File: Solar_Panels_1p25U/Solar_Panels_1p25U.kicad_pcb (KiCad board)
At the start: 2 copper layers, 113 x 82.5 mm, 62 parts, among them J1 Conn_01x08_MountingPin, J2 Conn_01x08_MountingPin, J3 Conn_01x08_MountingPin, J4 Conn_01x02, J5 Conn_01x08_MountingPin

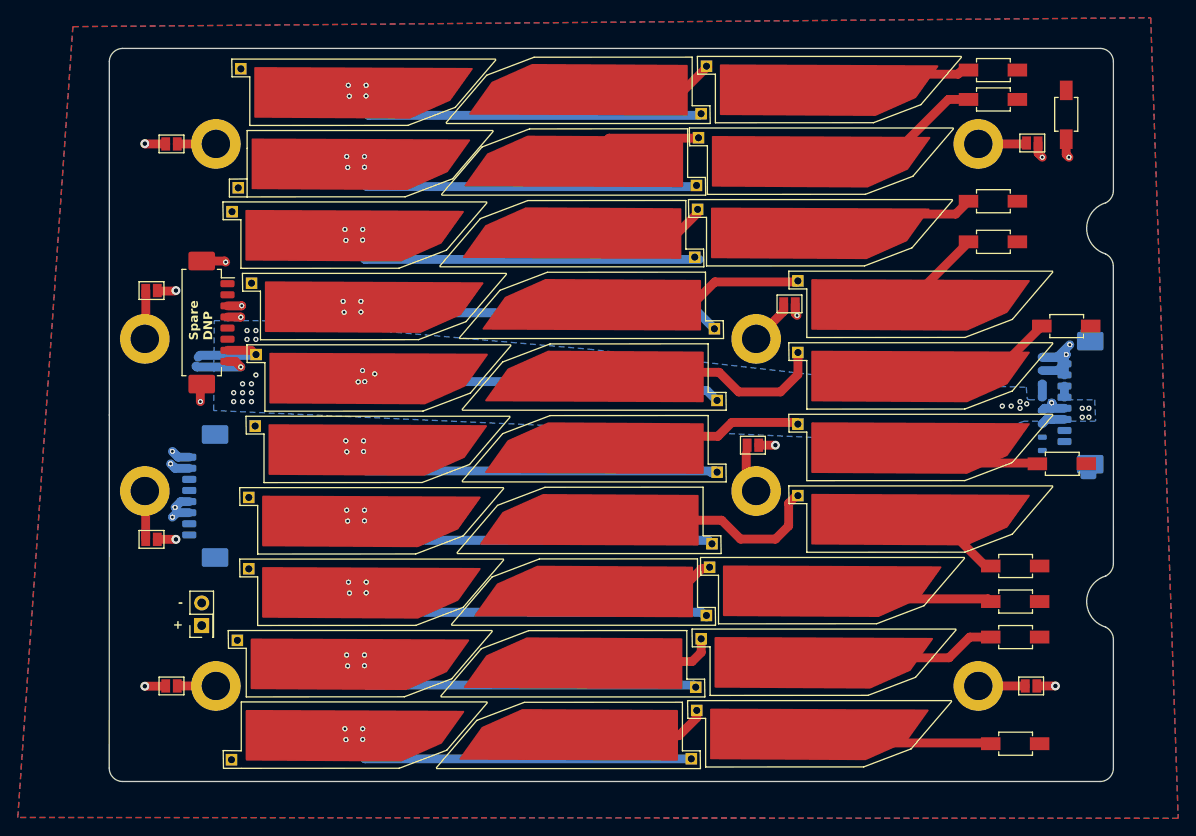
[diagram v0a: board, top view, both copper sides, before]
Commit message: Design new Rev 2 solar panel with new cells
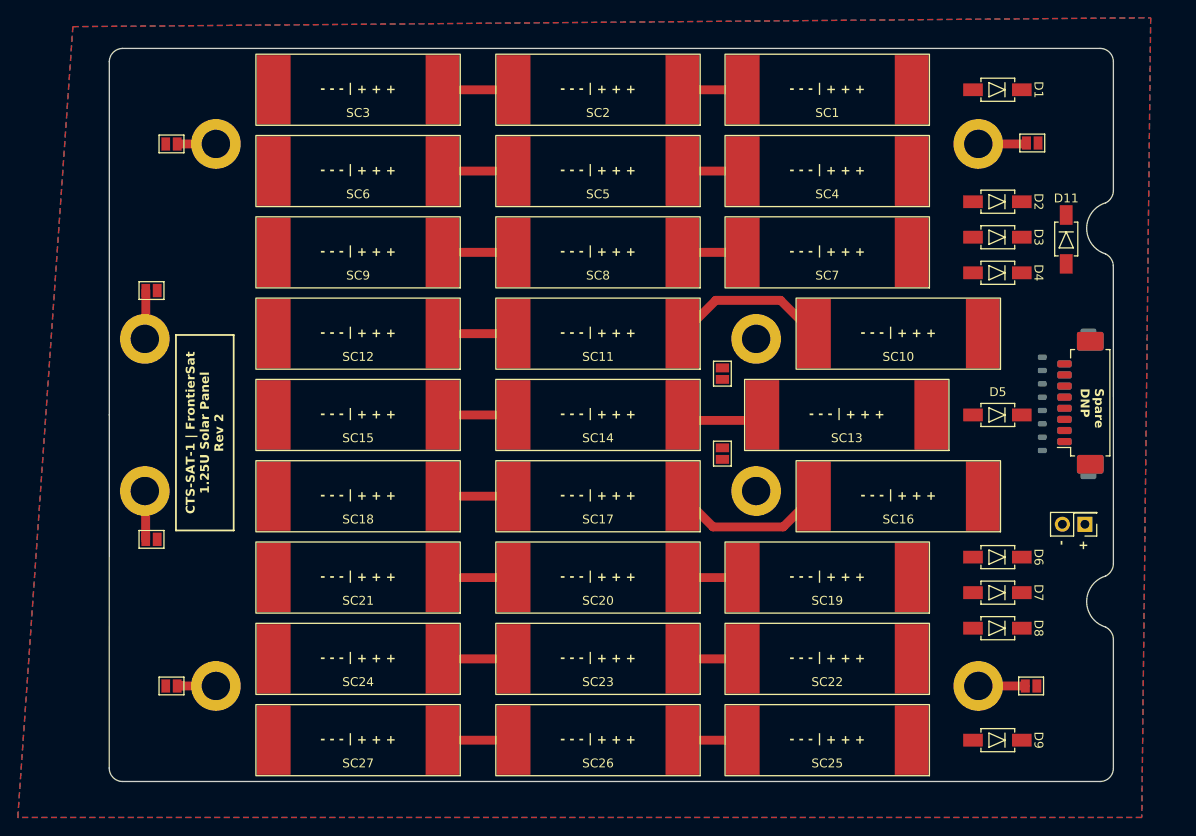
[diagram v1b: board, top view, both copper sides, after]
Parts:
- removed D10: PMEG10020AELPX, Solar Panel Library:PMEG10020AELPX
- removed J2: Conn_01x08_MountingPin, Connector_Molex:Molex_PicoBlade_53261-0871_1x08-1MP_P1.25mm_Horizontal
- removed SC28, SC29, SC30: Solar_Cell, Solar Panel Library:TrisolX Solar Wings
- SC1, SC10, SC11, SC12, SC13, SC14, SC15, SC16, SC17, SC18, SC19, SC2, SC20, SC21, SC22, SC23, SC24, SC25, SC26, SC27, SC3, SC4, SC5, SC6, SC7, SC8, SC9: footprint Solar Panel Library:TrisolX Solar Wings -> Solar Panel Library:KXOB25-05X3F
- moved J4 100.1 mm to (184.8, 128.3), turned to 180 degrees
- moved J3 99.4 mm to (184.9, 114.6), turned to 90 degrees
- moved D11 14.0 mm to (182.7, 96.2)
- moved D6 12.8 mm to (175.0, 132.0)
- moved D5 12.7 mm to (175.0, 116.0)
- moved D9 11.8 mm to (175.0, 152.6)
- moved D2 11.5 mm to (175.0, 92.0)
- moved JP5 10.9 mm to (144.0, 111.3), turned to -90 degrees
- moved SC19 9.85 mm to (155.8, 134.3), turned to 180 degrees
- moved SC25 9.64 mm to (155.8, 152.6), turned to 180 degrees
- moved SC27 9.27 mm to (103.0, 152.6), turned to 180 degrees
- moved SC26 8.48 mm to (130.0, 152.6), turned to 180 degrees
- moved SC22 8.28 mm to (155.8, 143.4), turned to 180 degrees
- moved SC24 7.84 mm to (103.0, 143.4), turned to 180 degrees
- moved SC23 7.58 mm to (130.0, 143.4), turned to 180 degrees
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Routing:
- net GND: track 45.0 -> 0.00 mm, vias 14 -> 0
- net Net-(SC29--): track 44.8 -> 0.00 mm, vias 4 -> 0
- net Net-(SC17--): track 47.3 -> 8.00 mm, vias 4 -> 0
- net Net-(SC20--): track 46.1 -> 8.00 mm, vias 4 -> 0
- net Net-(SC14--): track 45.4 -> 8.00 mm, vias 4 -> 0
- net Net-(SC23--): track 45.3 -> 8.00 mm, vias 4 -> 0
- net Net-(SC11--): track 44.8 -> 8.00 mm, vias 4 -> 0
- net Net-(SC2--): track 44.7 -> 8.00 mm, vias 4 -> 0
- net Net-(SC8--): track 44.7 -> 8.00 mm, vias 4 -> 0
- net Net-(SC5--): track 44.2 -> 8.00 mm, vias 4 -> 0
- net Net-(SC26--): track 44.2 -> 8.00 mm, vias 4 -> 0
- net +VDC: track 26.1 -> 0.00 mm, vias 29 -> 0
- net Net-(SC25-+): track 21.6 -> 0.00 mm
- net Net-(SC22-+): track 21.2 -> 0.00 mm
- net Net-(SC4-+): track 19.0 -> 0.00 mm
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- added copper zone on F.Cu, net GND
- removed copper zone on B.Cu, net +VDC
- removed copper zone on F.Cu, net +VDC
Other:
- board text added: "CTS-SAT-1 | FrontierSat 1.25U Solar Panel Rev 2"
- board text added: "Stackup: 2 layers. 1.6mm FR4 PCB. All polygon pours: GND"
- board text removed: "Pre-Order Checks: * Hide reference designators. * Check that current can flow across the board in the top layer pour. A blue-layer polygon helps add extra current-carrying capacity across the board. * DRC."
- board text removed: "Stackup: 2 layers. 1.6mm FR4 PCB. Top (Red): +VDC Bottom (Blue): GND"

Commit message: Finish routing
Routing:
- net +VDC: track 0.00 -> 137.1 mm, vias 0 -> 4
- net Net-(SC4-+): track 0.00 -> 8.33 mm
- net Net-(SC22-+): track 0.00 -> 8.33 mm
- net Net-(SC7-+): track 0.00 -> 7.60 mm
- net Net-(SC19-+): track 0.00 -> 7.60 mm
- net Net-(SC16-+): track 0.00 -> 7.31 mm
- net Net-(SC10-+): track 0.00 -> 7.31 mm
- net Net-(SC25-+): track 0.00 -> 6.90 mm
- net Net-(SC1-+): track 0.00 -> 6.90 mm
- net Net-(JP6-A): track 0.00 -> 5.27 mm
- net Net-(JP5-A): track 0.00 -> 5.15 mm
- net Net-(SC13-+): track 0.00 -> 4.70 mm

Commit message: Update footprints with extra protuding pads for testing
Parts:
- removed D1, D3, D5, D7: PMEG10020AELPX, Solar Panel Library:PMEG10020AELPX
- added SC28: KXOB25-05X3F, Solar Panel Library:KXOB25-05X3F, F.Cu at (86.5, 129.0)
- added SC29: KXOB25-05X3F, Solar Panel Library:KXOB25-05X3F, F.Cu at (86.5, 103.0)
- added SC30: KXOB25-05X3F, Solar Panel Library:KXOB25-05X3F, F.Cu at (180.5, 143.5)
- SC1, SC10, SC11, SC12, SC13, SC14, SC15, SC16, SC17, SC18, SC19, SC2, SC20, SC21, SC22, SC23, SC24, SC25, SC26, SC27, SC3, SC4, SC5, SC6, SC7, SC8, SC9: value Solar_Cell -> KXOB25-05X3F
- moved SC13 55.0 mm to (103.0, 116.0), turned to 0 degrees
- moved SC15 55.0 mm to (158.0, 116.0), turned to 0 degrees
- moved SC1 52.8 mm to (103.0, 79.4), turned to 0 degrees
- moved SC19 52.8 mm to (103.0, 134.3), turned to 0 degrees
- moved SC3 52.8 mm to (155.8, 79.4), turned to 0 degrees
- moved SC7 52.8 mm to (103.0, 97.7), turned to 0 degrees
- moved SC9 52.8 mm to (155.8, 97.7), turned to 0 degrees
- moved SC21 50.2 mm to (153.2, 134.3), turned to 0 degrees
- moved D9 25.8 mm to (178.5, 127.0), turned to -90 degrees
- moved D6 13.0 mm to (175.0, 119.0)
- moved JP8 10.7 mm to (168.0, 146.5), turned to 90 degrees
- moved JP3 7.43 mm to (87.0, 80.0)
- moved JP4 7.11 mm to (87.5, 151.0), turned to 0 degrees
- moved D8 5.00 mm to (170.0, 140.0)
- moved SC22 2.60 mm to (153.2, 143.4)
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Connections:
- D9 pad 2: Net-(SC25-+) -> Net-(SC30-+)
- SC12 pad 2: GND -> Net-(SC12--)
- SC18 pad 2: GND -> Net-(SC13-+)
- SC24 pad 2: GND -> Net-(SC19-+)
- SC27 pad 2: GND -> Net-(SC27--)
- SC6 pad 2: GND -> Net-(SC1-+)
- SC7 pad 1: Net-(SC7-+) -> Net-(SC12--)
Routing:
- net +VDC: track 137.1 -> 101.2 mm
- net Net-(SC27--): track 0.00 -> 28.0 mm
- net Net-(SC25-+): track 6.90 -> 18.0 mm
- net Net-(SC12--): track 0.00 -> 9.15 mm
- net Net-(SC7-+): track 7.60 -> 0.00 mm
- net Net-(SC28--): track 0.00 -> 7.00 mm
- net Net-(SC30-+): track 0.00 -> 5.03 mm
- net Net-(SC13-+): track 4.70 -> 9.15 mm
- net Net-(SC1-+): track 6.90 -> 9.15 mm
- net Net-(SC20--): track 8.00 -> 6.00 mm
- net Net-(JP4-A): track 3.39 -> 5.27 mm
- net Net-(SC26--): track 8.00 -> 6.20 mm
- net Net-(SC23--): track 8.00 -> 6.20 mm
- net Net-(SC19-+): track 7.60 -> 9.15 mm
- net Net-(SC22-+): track 8.33 -> 6.81 mm
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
